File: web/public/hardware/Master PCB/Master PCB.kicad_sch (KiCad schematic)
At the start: 28 parts, among them J1 SWD Conn, J2 OLED1, J3 OLED2, J4 5V_IN

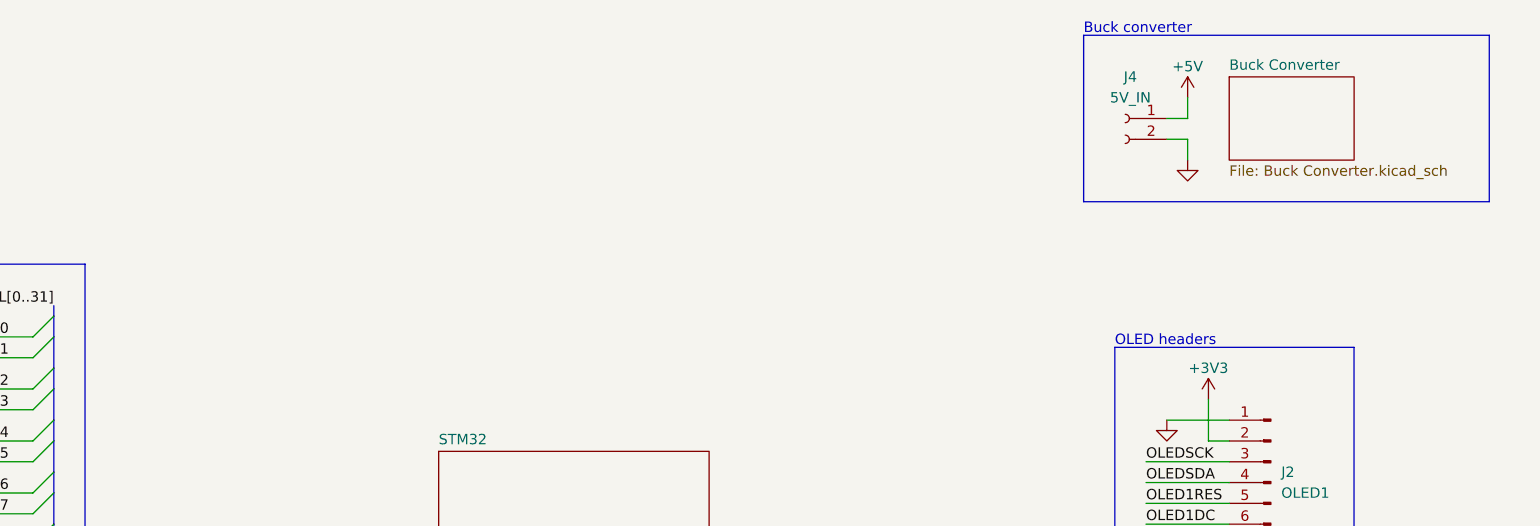
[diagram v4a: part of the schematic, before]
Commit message: Add goal detection
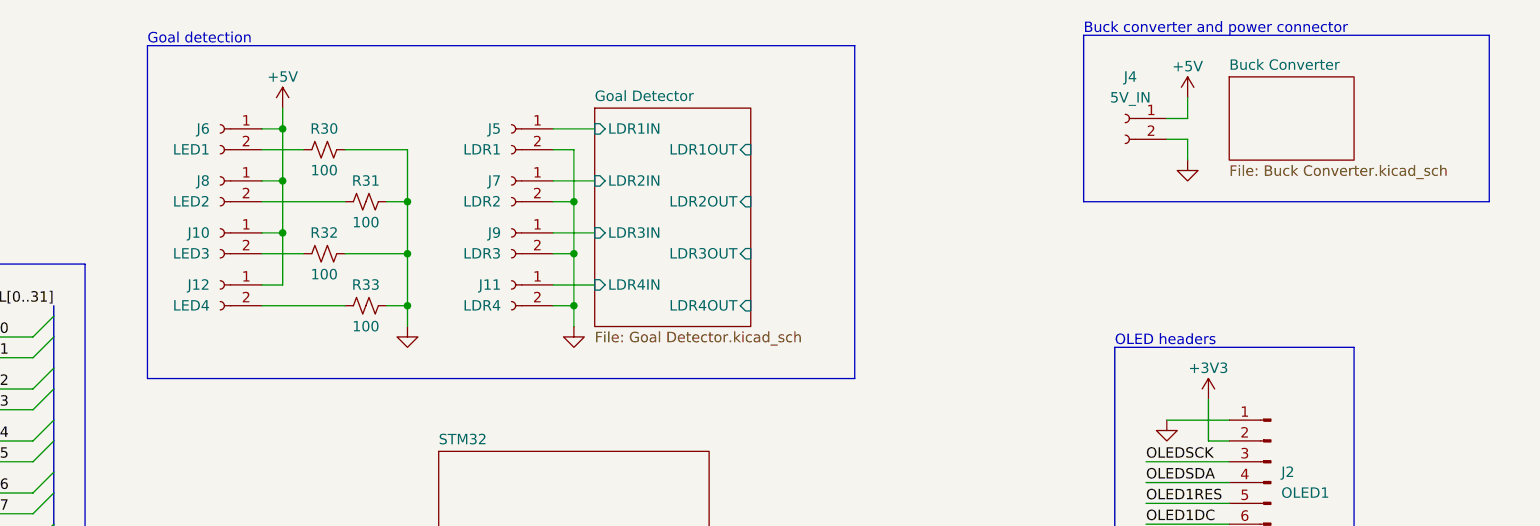
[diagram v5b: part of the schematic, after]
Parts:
- added J10: LED3, symbol Connector:Conn_01x02_Socket
- added J11: LDR4, symbol Connector:Conn_01x02_Socket
- added J12: LED4, symbol Connector:Conn_01x02_Socket
- added J5: LDR1, symbol Connector:Conn_01x02_Socket
- added J6: LED1, symbol Connector:Conn_01x02_Socket
- added J7: LDR2, symbol Connector:Conn_01x02_Socket
- added J8: LED2, symbol Connector:Conn_01x02_Socket
- added J9: LDR3, symbol Connector:Conn_01x02_Socket
- added R30, R31, R32, R33: 100, symbol Device:R_Small_US
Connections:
- net +5V: now also J10.1 (Pin_1), J12.1 (Pin_1), J6.1 (Pin_1), J8.1 (Pin_1)
- net GND: now also J11.2 (Pin_2), J5.2 (Pin_2), J7.2 (Pin_2), J9.2 (Pin_2), R30.2, R31.2, R32.2, R33.2
- new net: J10.2 (Pin_2), R32.1
- new net: J12.2 (Pin_2), R33.1
- new net: J6.2 (Pin_2), R30.1
- new net: J8.2 (Pin_2), R31.1
- new net Goal Detector/LDR1IN: J5.1 (Pin_1)
- new net Goal Detector/LDR2IN: J7.1 (Pin_1)
- new net Goal Detector/LDR3IN: J9.1 (Pin_1)
- new net Goal Detector/LDR4IN: J11.1 (Pin_1)
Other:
- added sheet Goal Detector (Goal Detector.kicad_sch)
- note added: "Buck converter and power connector"
- note added: "Goal detection"
- note removed: "Buck converter"

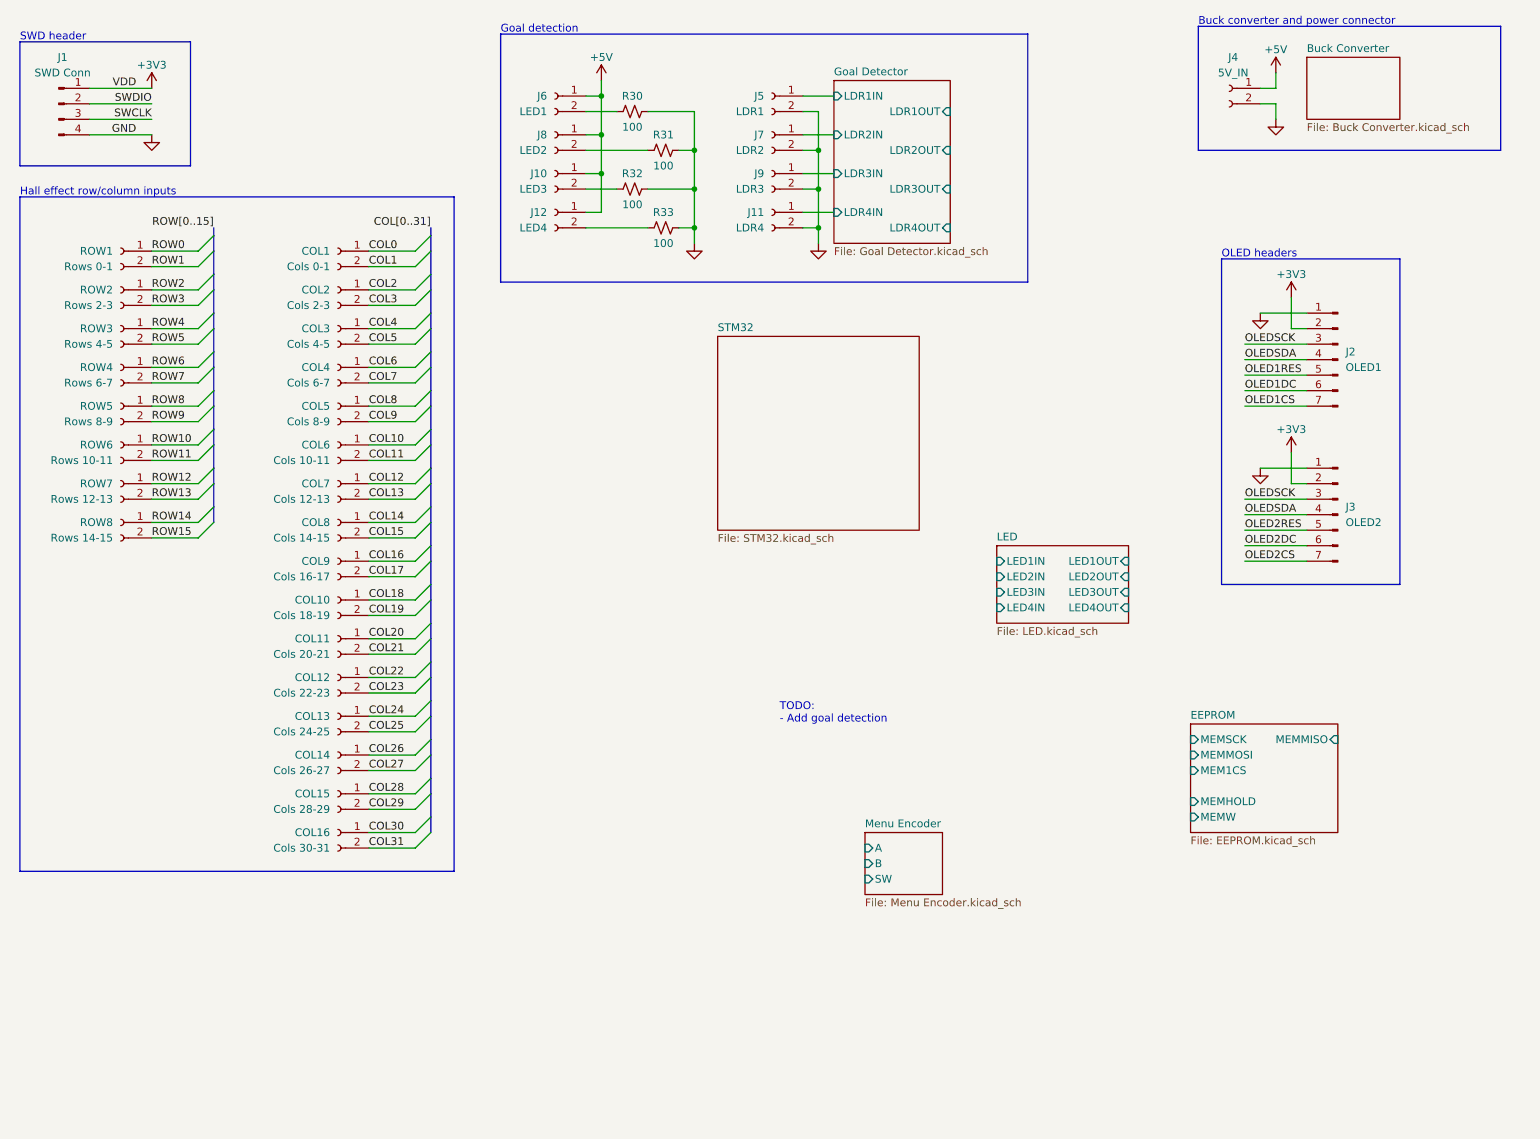
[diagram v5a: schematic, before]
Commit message: Rearrange schematic
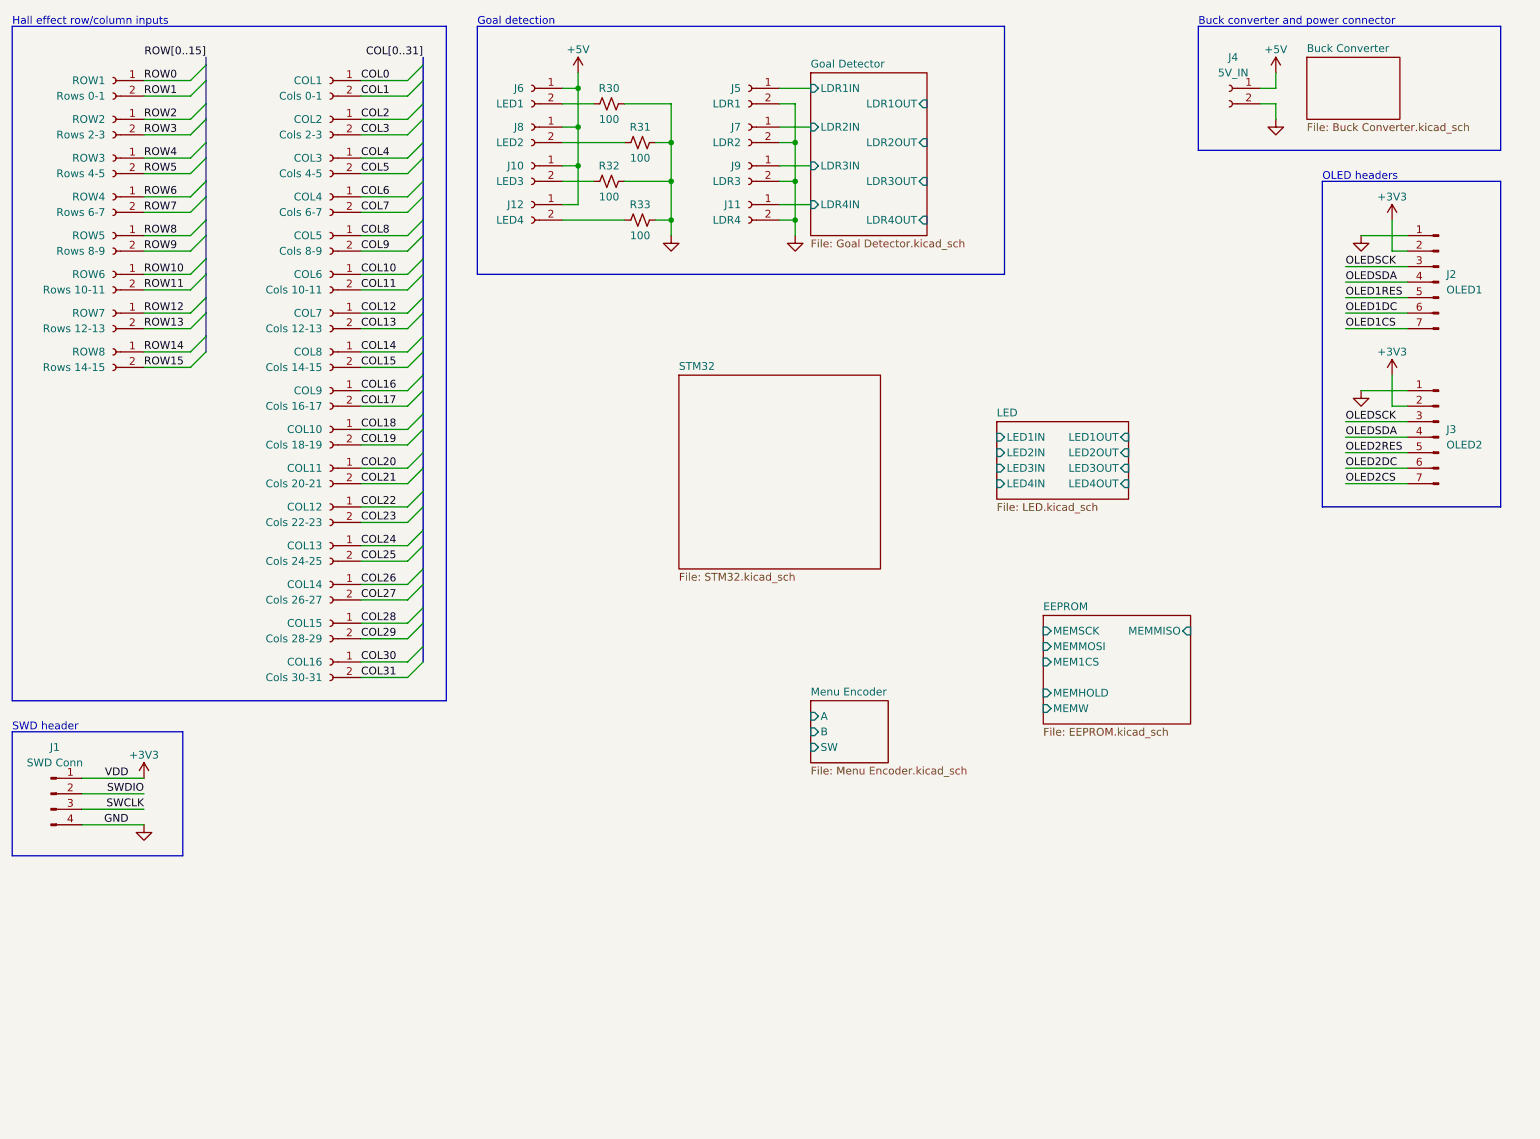
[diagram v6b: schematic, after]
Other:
- note removed: "TODO: - Add goal detection"
- moved on the sheet: COL1, COL10, COL11, COL12, COL13, COL14, COL15, COL16, COL2, COL3, COL4, COL5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

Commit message: Finish schematic and start routing PCB
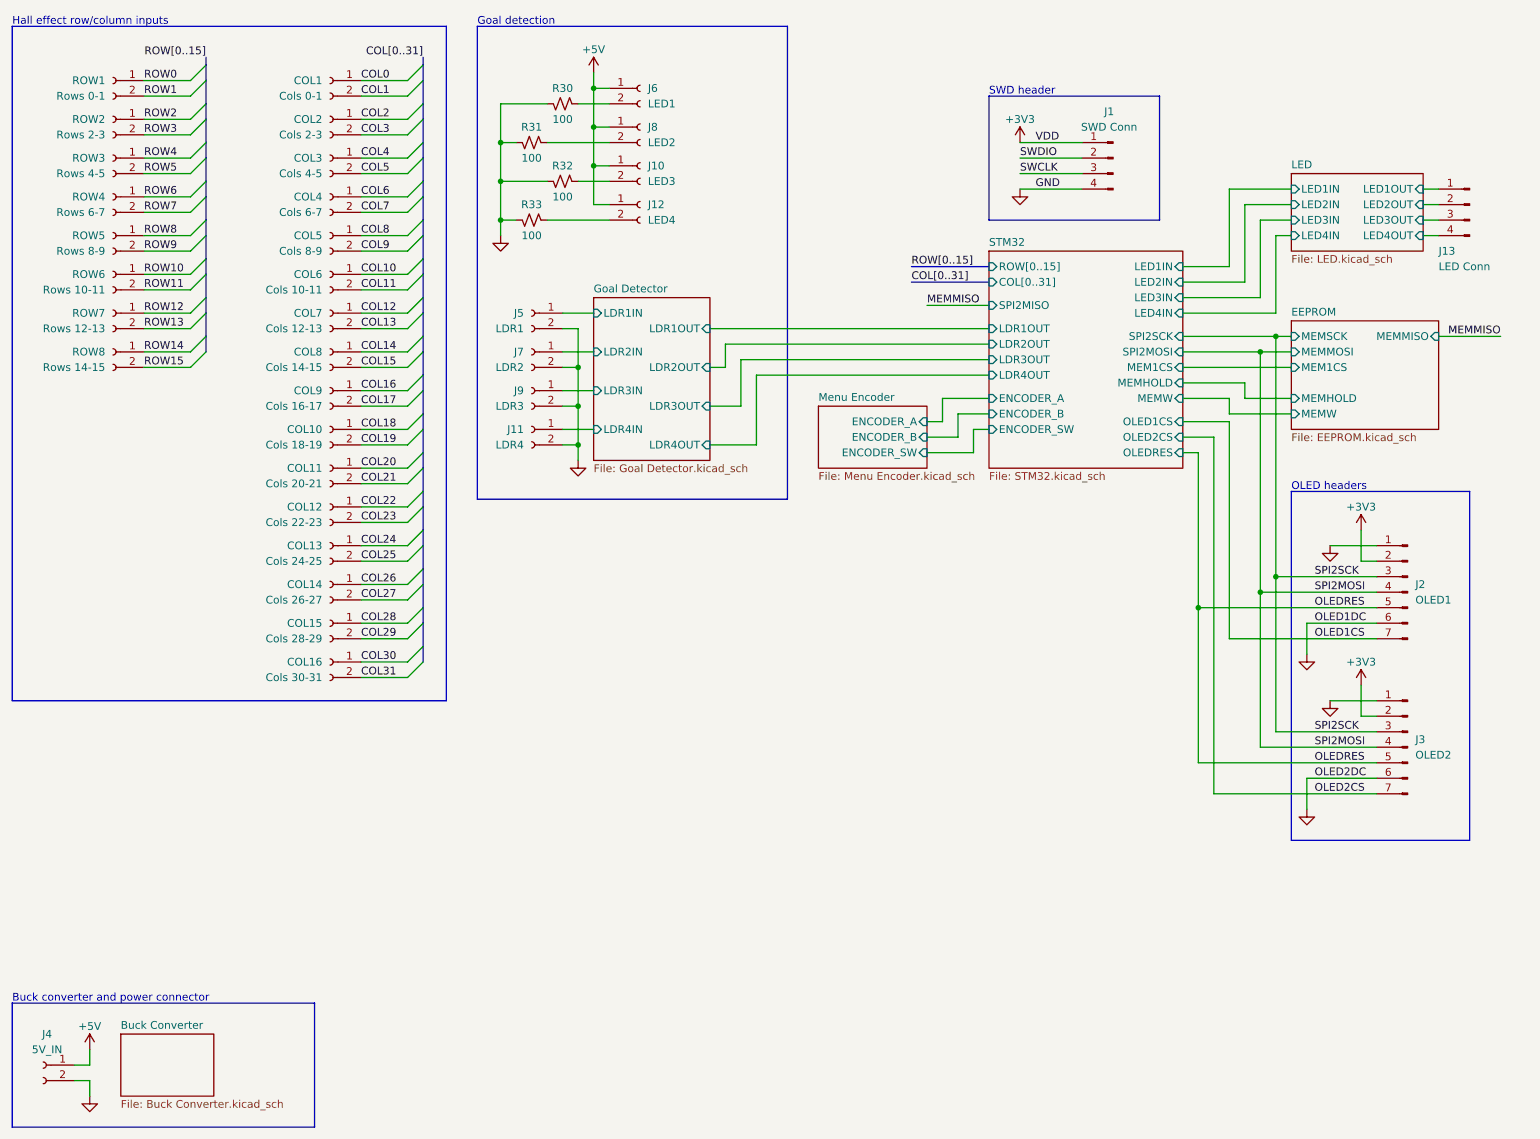
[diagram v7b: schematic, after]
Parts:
- added J13: LED Conn, Connector_PinHeader_2.54mm:PinHeader_1x04_P2.54mm_Vertical, symbol Connector:Conn_01x04_Pin
- COL1, COL10, COL11, COL12, COL13, COL14, COL15, COL16, COL2, COL3, COL4, COL5, COL6, COL7, COL8, COL9, J10, J11, J12, J4, J5, J6, J7, J8, J9, ROW1, ROW2, ROW3, ROW4, ROW5, ROW6, ROW7, ROW8: footprint (none) -> Connector_PinHeader_2.54mm:PinHeader_1x02_P2.54mm_Vertical
- J1: footprint (none) -> Connector_PinHeader_2.54mm:PinHeader_1x04_P2.54mm_Vertical
- J2, J3: footprint (none) -> Connector_PinHeader_2.54mm:PinHeader_1x07_P2.54mm_Vertical
- R30, R31, R32, R33: footprint (none) -> Resistor_SMD:R_0805_2012Metric_Pad1.20x1.40mm_HandSolder
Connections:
- net OLED1DC is gone; now on net GND: J2.6 (Pin_6)
- net OLED2DC is gone; now on net GND: J3.6 (Pin_6)
- net OLED2RES is gone; now on net OLEDRES: J3.5 (Pin_5)
- net LED/LED1OUT: now also J13.1 (Pin_1)
- net LED/LED2OUT: now also J13.2 (Pin_2)
- net LED/LED3OUT: now also J13.3 (Pin_3)
- net LED/LED4OUT: now also J13.4 (Pin_4)
- net OLED1RES renamed OLEDRES
- net OLEDSCK renamed SPI2SCK
- net OLEDSDA renamed SPI2MOSI
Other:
- sheet Menu Encoder ports: added ENCODER_A, ENCODER_B, ENCODER_SW; removed A, B, SW
- sheet STM32 ports: added COL[0..31], ENCODER_A, ENCODER_B, ENCODER_SW, LDR1OUT, LDR2OUT, LDR3OUT, LDR4OUT, LED1IN, LED2IN, LED3IN, LED4IN, MEM1CS, MEMHOLD, MEMW, OLED1CS, OLED2CS, OLEDRES, ROW[0..15], SPI2MISO, SPI2MOSI, SPI2SCK; removed none
- moved on the sheet: J1, J10, J11, J12, J2, J3, J4, J5, J6, J7, J8, J9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
